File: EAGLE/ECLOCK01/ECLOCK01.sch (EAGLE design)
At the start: 12 parts

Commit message: FInal version of clock PCB before sending to board house
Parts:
- removed JP1: POWER_JACKCOMBO, SparkFun-Connectors:POWER_JACKCOMBO
- removed L1, L2, L3, L4: WS2812B, adafruit:WS2812B
- added C10, C11, C12, C13, C14, C15, C16, C17, C18, C19, C20, C21, C22, C23, C24, C25, C26, C27, C28, C29, C30, C31, C32, C33, C34, C35, C36, C37, C38, C39, C41, C42, C43, C44, C45, C46, C47, C48, C49, C50, C51, C52, C53, C54, C6, C7, C8, C9: 0.1, TinWhiskers:CAPACITOR0805
- added C400, C401: 470, adafruit:CPOL-USE
- added FID1, FID2: FIDUCIAL, TinWhiskers:FIDUCIAL
- added JP2: USB-MICROB, SparkFun-Connectors:USB-MICROB
- added LED1, LED10, LED11, LED12, LED13, LED14, LED15, LED16, LED17, LED18, LED19, LED2, LED20, LED21, LED22, LED23, LED24, LED25, LED26, LED27, LED28, LED29, LED3, LED30, LED31, LED32, LED33, LED34, LED35, LED36, LED37, LED38, LED39, LED4, LED40, LED41, LED42, LED43, LED44, LED45, LED46, LED47, LED48, LED49, LED5, LED50, LED51, LED52, LED53, LED54, LED6, LED7, LED8, LED9: WS2812B, GinWhiskers - temp stuff:WS2812B
- C1, C2, C3: value CAPACITOR0805 -> 0.1
- C4, C5: value 470 -> 0.1; device adafruit:CPOL-USE -> TinWhiskers:CAPACITOR0805
- U$1: device adafruit:ARDUINOUNO -> GinWhiskers - temp stuff:ARDUINOUNO
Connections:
- removed net N$6: L3.DOUT, L4.DIN
- new net N$10: LED15.DOUT, LED16.DIN
- new net N$12: LED18.DIN, LED53.DOUT
- new net N$13: LED19.DOUT, LED20.DIN
- new net N$14: LED17.DIN, LED18.DOUT
- new net N$15: LED19.DIN, LED8.DOUT
- new net N$16: LED47.DOUT, LED49.DIN
- new net N$17: LED39.DOUT, LED50.DIN
- new net N$18: LED24.DOUT, LED25.DIN
- new net N$19: LED25.DOUT, LED26.DIN
- new net N$2: LED11.DOUT, LED12.DIN
- new net N$20: LED13.DOUT, LED24.DIN
- new net N$21: LED27.DOUT, LED28.DIN
- new net N$22: LED28.DOUT, LED29.DIN
- new net N$25: LED40.DOUT, LED41.DIN
- new net N$26: LED20.DOUT, LED21.DIN
- new net N$27: LED11.DIN, LED9.DOUT
- new net N$28: LED17.DOUT, LED5.DIN
- new net N$29: LED4.DIN, LED5.DOUT
- new net N$30: LED6.DOUT, LED7.DIN
- new net N$31: LED7.DOUT, LED8.DIN
- new net N$32: LED21.DOUT, LED32.DIN
- new net N$33: LED48.DIN, LED49.DOUT
- new net N$34: LED36.DIN, LED48.DOUT
- new net N$36: LED37.DOUT, LED38.DIN
- new net N$37: LED38.DOUT, LED39.DIN
- new net N$39: LED30.DOUT, LED53.DIN
- new net N$40: LED34.DOUT, LED45.DIN
- new net N$41: LED32.DOUT, LED33.DIN
- new net N$42: LED33.DOUT, LED34.DIN
- new net N$44: LED31.DIN, LED43.DOUT
- new net N$45: LED4.DOUT, LED6.DIN
- new net N$46: LED46.DOUT, LED47.DIN
- new net N$47: LED45.DOUT, LED46.DIN
- new net N$48: LED42.DOUT, LED44.DIN
- new net N$49: LED43.DIN, LED44.DOUT
- new net N$50: LED30.DIN, LED31.DOUT
- new net N$51: LED41.DOUT, LED42.DIN
- new net N$52: LED35.DIN, LED36.DOUT
- new net N$53: LED35.DOUT, LED54.DIN
- new net N$54: LED50.DOUT, LED51.DIN
- new net N$55: LED51.DOUT, LED52.DIN
- new net N$56: LED23.DIN, LED54.DOUT
- new net N$58: LED22.DIN, LED23.DOUT
- new net N$59: LED14.DIN, LED3.DOUT
- new net N$60: LED10.DIN, LED22.DOUT
- new net N$61: LED10.DOUT, LED9.DIN
- new net N$62: LED29.DOUT, LED40.DIN
- new net N$7: LED12.DOUT, LED13.DIN
- new net N$8: LED26.DOUT, LED37.DIN
- new net N$9: LED14.DOUT, LED15.DIN
- new net VDD: C1.1, C10.1, C11.1, C12.1, C13.1, C14.1, C15.1, C16.1, C17.1, C18.1, C19.1, C2.1, C20.1, C21.1, C22.1, C23.1, C24.1, C25.1, C26.1, C27.1, C28.1, C29.1, C3.1, C30.1, C31.1, C32.1, C33.1, C34.1, C35.1, C36.1, C37.1, C38.1, C39.1, C4.1, C400.+, C401.+, C41.1, C42.1, C43.1, C44.1, C45.1, C46.1, C47.1, C48.1, C49.1, C5.1, C50.1, C51.1, C52.1, C53.1, C54.1, C6.1, C7.1, C8.1, C9.1, JP2.VBUS, LED1.VDD, LED10.VDD, LED11.VDD, LED12.VDD, LED13.VDD, LED14.VDD, LED15.VDD, LED16.VDD, LED17.VDD, LED18.VDD, LED19.VDD, LED2.VDD, LED20.VDD, LED21.VDD, LED22.VDD, LED23.VDD, LED24.VDD, LED25.VDD, LED26.VDD, LED27.VDD, LED28.VDD, LED29.VDD, LED3.VDD, LED30.VDD, LED31.VDD, LED32.VDD, LED33.VDD, LED34.VDD, LED35.VDD, LED36.VDD, LED37.VDD, LED38.VDD, LED39.VDD, LED4.VDD, LED40.VDD, LED41.VDD, LED42.VDD, LED43.VDD, LED44.VDD, LED45.VDD, LED46.VDD, LED47.VDD, LED48.VDD, LED49.VDD, LED5.VDD, LED50.VDD, LED51.VDD, LED52.VDD, LED53.VDD, LED54.VDD, LED6.VDD, LED7.VDD, LED8.VDD, LED9.VDD
- net GND: now also C1.2, C10.2, C11.2, C12.2, C13.2, C14.2, C15.2, C16.2, C17.2, C18.2, C19.2, C2.2, C20.2, C21.2, C22.2, C23.2, C24.2, C25.2, C26.2, C27.2, C28.2, C29.2, C3.2, C30.2, C31.2, C32.2, C33.2, C34.2, C35.2, C36.2, C37.2, C38.2, C39.2, C4.2, C400.-, C401.-, C41.2, C42.2, C43.2, C44.2, C45.2, C46.2, C47.2, C48.2, C49.2, C5.2, C50.2, C51.2, C52.2, C53.2, C54.2, C6.2, C7.2, C8.2, C9.2, JP2.GND, LED1.GND, LED10.GND, LED11.GND, LED12.GND, LED13.GND, LED14.GND, LED15.GND, LED16.GND, LED17.GND, LED18.GND, LED19.GND, LED2.GND, LED20.GND, LED21.GND, LED22.GND, LED23.GND, LED24.GND, LED25.GND, LED26.GND, LED27.GND, LED28.GND, LED29.GND, LED3.GND, LED30.GND, LED31.GND, LED32.GND, LED33.GND, LED34.GND, LED35.GND, LED36.GND, LED37.GND, LED38.GND, LED39.GND, LED4.GND, LED40.GND, LED41.GND, LED42.GND, LED43.GND, LED44.GND, LED45.GND, LED46.GND, LED47.GND, LED48.GND, LED49.GND, LED5.GND, LED50.GND, LED51.GND, LED52.GND, LED53.GND, LED54.GND, LED6.GND, LED7.GND, LED8.GND, LED9.GND; no longer C4.-, C5.-, JP1.GND, JP1.GNDBREAK, L1.GND, L2.GND, L3.GND, L4.GND
- net LED_IN: now also U$1.D13; no longer U$1.D0
- net N$1: now also LED1.DIN; no longer L1.DIN
- net N$3: now also LED1.DOUT, LED2.DIN; no longer L1.DOUT, L2.DIN
- net N$4: now also LED2.DOUT, LED3.DIN; no longer L2.DOUT, L3.DIN
- net N$5: now also LED16.DOUT, LED27.DIN; no longer C4.+, C5.+, JP1.PWR, L1.VDD, L2.VDD, L3.VDD, L4.VDD

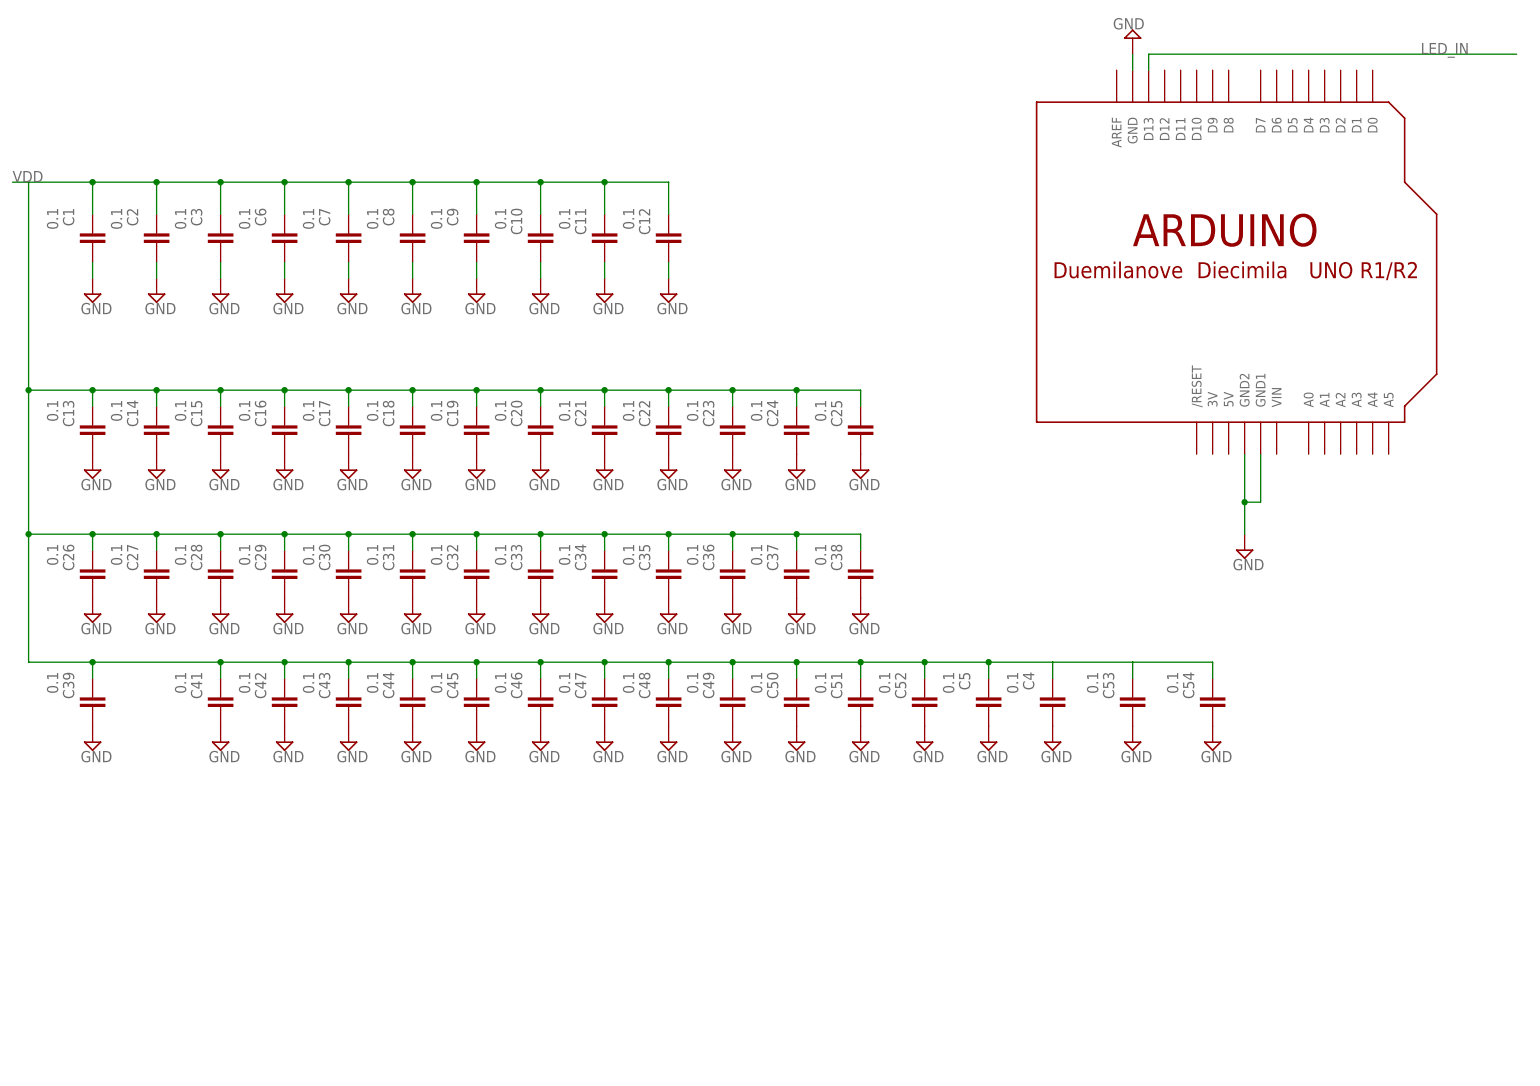
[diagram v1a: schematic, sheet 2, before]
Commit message: Added two pushbuttons and a connector for the horn
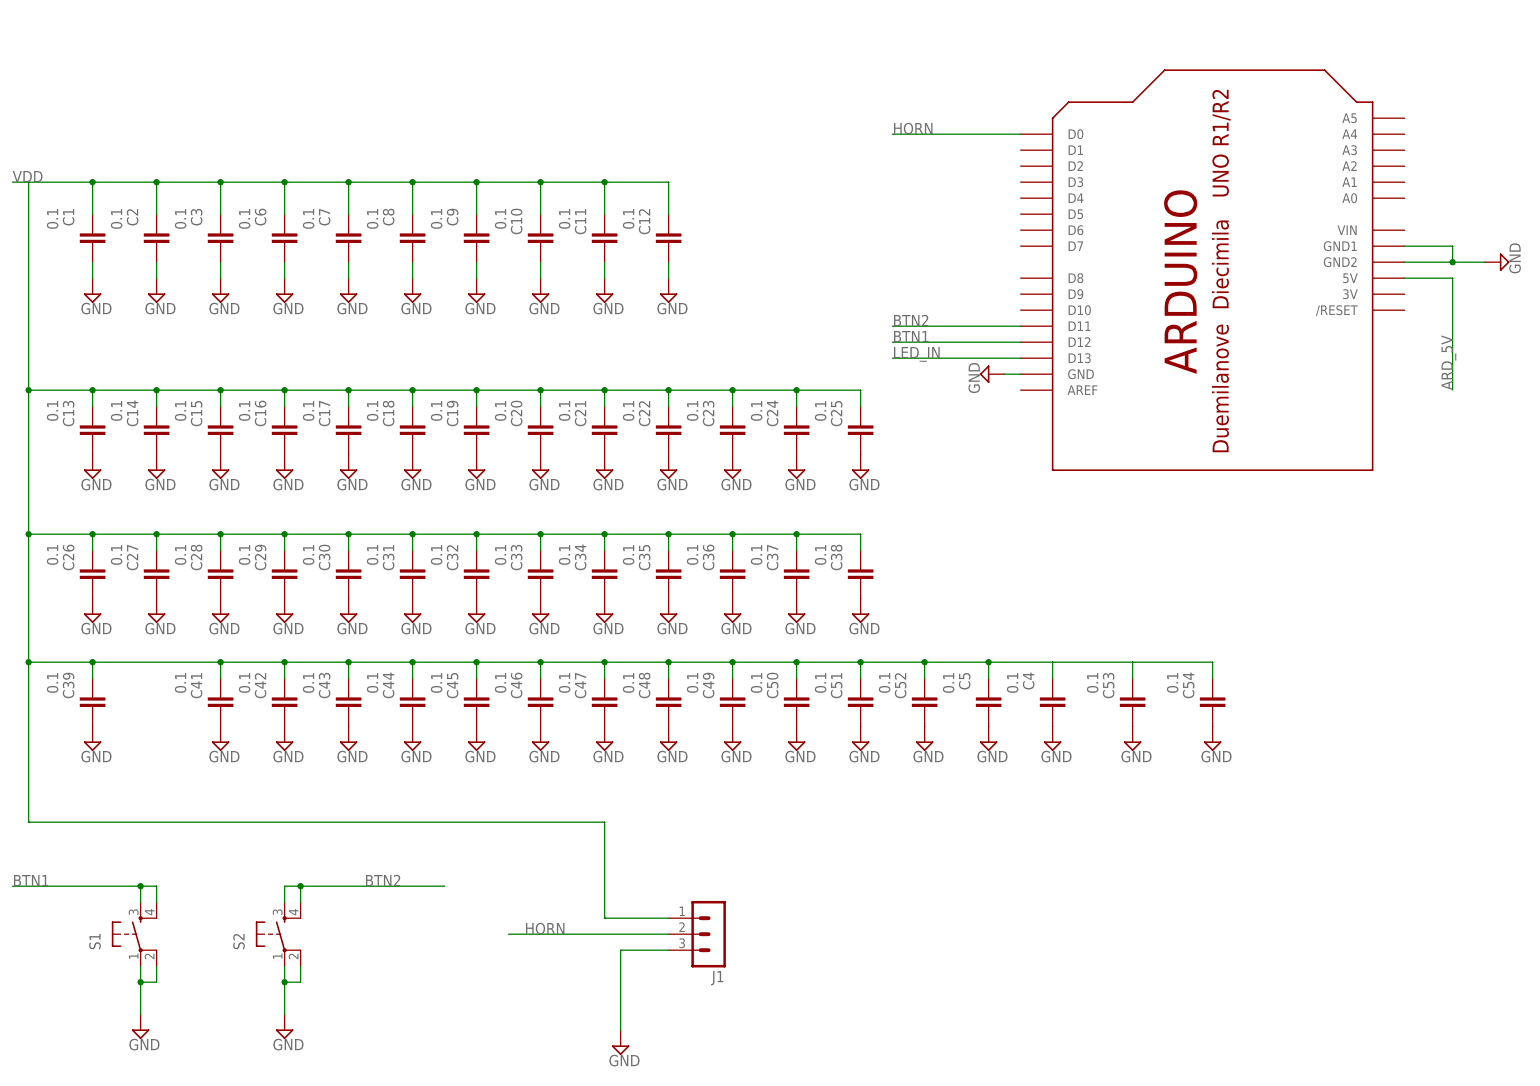
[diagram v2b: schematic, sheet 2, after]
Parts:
- added J1: (no value), !con-lstb:MA03-1
- added S1, S2: (no value), SparkFun:TAC_SWITCHSMD
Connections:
- new net ARD_5V: U$1.5V
- new net BTN1: S1.3, S1.4, U$1.D12
- new net BTN2: S2.3, S2.4, U$1.D11
- new net HORN: J1.2, U$1.D0
- net GND: now also J1.3, S1.1, S1.2, S2.1, S2.2
- net VDD: now also J1.1
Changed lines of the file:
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@@
 </variantdefs>
 <classes>
-<class number="0" name="default" width="0" drill="0">
+<class number="0" name="default" width="0.1524" drill="0.3048">
+<clearance class="0" value="0.1524"/>
+</class>
+<class number="1" name="power" width="0" drill="0">
 </class>
 </classes>
@@
 <part name="SUPPLY112" library="TinWhiskers" deviceset="GND" device=""/>
 <part name="SUPPLY113" library="TinWhiskers" deviceset="GND" device=""/>
+<part name="S1" library="SparkFun" deviceset="TAC_SWITCH" device="SMD"/>
+<part name="S2" library="SparkFun" deviceset="TAC_SWITCH" device="SMD"/>
+<part name="SUPPLY97" library="TinWhiskers" deviceset="GND" device=""/>
+<part name="SUPPLY114" library="TinWhiskers" deviceset="GND" device=""/>
+<part name="J1" library="!con-lstb" deviceset="MA03-1" device=""/>
+<part name="SUPPLY115" library="TinWhiskers" deviceset="GND" device=""/>
 </parts>
 <sheets>
@@
 </plain>
 <instances>
-<instance part="U$1" gate="G$1" x="208.28" y="134.62"/>
-<instance part="SUPPLY8" gate="GND" x="208.28" y="88.9"/>
-<instance part="SUPPLY9" gate="GND" x="190.5" y="170.18" rot="R180"/>
+<instance part="U$1" gate="G$1" x="203.2" y="134.62" rot="R90"/>
+<instance part="SUPPLY8" gate="GND" x="248.92" y="134.62" rot="R90"/>
+<instance part="SUPPLY9" gate="GND" x="167.64" y="116.84" rot="R270"/>
 <instance part="FRAME2" gate="G$1" x="0" y="0"/>
 <instance part="C13" gate="G$1" x="25.4" y="106.68" rot="R270"/>
@@
 <instance part="SUPPLY112" gate="GND" x="190.5" y="58.42"/>
 <instance part="SUPPLY113" gate="GND" x="203.2" y="58.42"/>
+<instance part="S1" gate="S" x="33.02" y="27.94" rot="R90"/>
+<instance part="S2" gate="S" x="55.88" y="27.94" rot="R90"/>
+<instance part="SUPPLY97" gate="GND" x="33.02" y="12.7"/>
+<instance part="SUPPLY114" gate="GND" x="55.88" y="12.7"/>
+<instance part="J1" gate="G$1" x="124.46" y="27.94" rot="R180"/>
+<instance part="SUPPLY115" gate="GND" x="109.22" y="10.16"/>
 </instances>
 <busses>
@@
 <pinref part="U$1" gate="G$1" pin="GND2"/>
 <pinref part="SUPPLY8" gate="GND" pin="GND"/>
-<wire x1="208.28" y1="104.14" x2="208.28" y2="96.52" width="0.1524" layer="91"/>
+<wire x1="233.68" y1="134.62" x2="241.3" y2="134.62" width="0.1524" layer="91"/>
 <pinref part="U$1" gate="G$1" pin="GND1"/>
-<wire x1="208.28" y1="96.52" x2="208.28" y2="91.44" width="0.1524" layer="91"/>
-<wire x1="210.82" y1="104.14" x2="210.82" y2="96.52" width="0.1524" layer="91"/>
-<wire x1="210.82" y1="96.52" x2="208.28" y2="96.52" width="0.1524" layer="91"/>
-<junction x="208.28" y="96.52"/>
+<wire x1="241.3" y1="134.62" x2="246.38" y2="134.62" width="0.1524" layer="91"/>
+<wire x1="233.68" y1="137.16" x2="241.3" y2="137.16" width="0.1524" layer="91"/>
+<wire x1="241.3" y1="137.16" x2="241.3" y2="134.62" width="0.1524" layer="91"/>
+<junction x="241.3" y="134.62"/>
 </segment>
 <segment>
 <pinref part="SUPPLY9" gate="GND" pin="GND"/>
 <pinref part="U$1" gate="G$1" pin="GND"/>
-<wire x1="190.5" y1="167.64" x2="190.5" y2="165.1" width="0.1524" layer="91"/>
+<wire x1="170.18" y1="116.84" x2="172.72" y2="116.84" width="0.1524" layer="91"/>
 </segment>
 <segment>
@@
 <pinref part="SUPPLY113" gate="GND" pin="GND"/>
 </segment>
+<segment>
+<pinref part="S1" gate="S" pin="1"/>
+<wire x1="33.02" y1="22.86" x2="33.02" y2="20.32" width="0.1524" layer="91"/>
+<pinref part="S1" gate="S" pin="2"/>
+<wire x1="33.02" y1="20.32" x2="35.56" y2="20.32" width="0.1524" layer="91"/>
+<wire x1="35.56" y1="20.32" x2="35.56" y2="22.86" width="0.1524" layer="91"/>
+<wire x1="33.02" y1="20.32" x2="33.02" y2="15.24" width="0.1524" layer="91"/>
+<pinref part="SUPPLY97" gate="GND" pin="GND"/>
+<junction x="33.02" y="20.32"/>
+</segment>
+<segment>
+<pinref part="S2" gate="S" pin="1"/>
+<wire x1="55.88" y1="22.86" x2="55.88" y2="20.32" width="0.1524" layer="91"/>
+<pinref part="S2" gate="S" pin="2"/>
+<wire x1="55.88" y1="20.32" x2="58.42" y2="20.32" width="0.1524" layer="91"/>
+<wire x1="58.42" y1="20.32" x2="58.42" y2="22.86" width="0.1524" layer="91"/>
+<wire x1="55.88" y1="20.32" x2="55.88" y2="15.24" width="0.1524" layer="91"/>
+<pinref part="SUPPLY114" gate="GND" pin="GND"/>
+<junction x="55.88" y="20.32"/>
+</segment>
+<segment>
+<pinref part="J1" gate="G$1" pin="3"/>
+<wire x1="116.84" y1="25.4" x2="109.22" y2="25.4" width="0.1524" layer="91"/>
+<wire x1="109.22" y1="25.4" x2="109.22" y2="12.7" width="0.1524" layer="91"/>
+<pinref part="SUPPLY115" gate="GND" pin="GND"/>
+</segment>
 </net>
 <net name="LED_IN" class="0">
 <segment>
-<label x="236.22" y="167.64" size="1.778" layer="95"/>
+<label x="152.4" y="119.38" size="1.778" layer="95"/>
 <pinref part="U$1" gate="G$1" pin="D13"/>
-<wire x1="251.46" y1="167.64" x2="193.04" y2="167.64" width="0.1524" layer="91"/>
-<wire x1="193.04" y1="167.64" x2="193.04" y2="165.1" width="0.1524" layer="91"/>
+<wire x1="152.4" y1="119.38" x2="172.72" y2="119.38" width="0.1524" layer="91"/>
 </segment>
 </net>
@@
 <wire x1="203.2" y1="68.58" x2="203.2" y2="71.12" width="0.1524" layer="91"/>
 <wire x1="203.2" y1="71.12" x2="190.5" y2="71.12" width="0.1524" layer="91"/>
-</segment>
-</net>
+<wire x1="116.84" y1="30.48" x2="106.68" y2="30.48" width="0.1524" layer="91"/>
+<wire x1="106.68" y1="30.48" x2="106.68" y2="45.72" width="0.1524" layer="91"/>
+<wire x1="106.68" y1="45.72" x2="15.24" y2="45.72" width="0.1524" layer="91"/>
+<wire x1="15.24" y1="45.72" x2="15.24" y2="71.12" width="0.1524" layer="91"/>
+<junction x="15.24" y="71.12"/>
+<pinref part="J1" gate="G$1" pin="1"/>
+</segment>
+</net>
+<net name="BTN2" class="0">
+<segment>
+<pinref part="S2" gate="S" pin="3"/>
+<wire x1="55.88" y1="33.02" x2="55.88" y2="35.56" width="0.1524" layer="91"/>
+<pinref part="S2" gate="S" pin="4"/>
+<wire x1="55.88" y1="35.56" x2="58.42" y2="35.56" width="0.1524" layer="91"/>
+<wire x1="58.42" y1="35.56" x2="58.42" y2="33.02" width="0.1524" layer="91"/>
+<wire x1="58.42" y1="35.56" x2="81.28" y2="35.56" width="0.1524" layer="91"/>
+<junction x="58.42" y="35.56"/>
+<label x="68.58" y="35.56" size="1.778" layer="95"/>
+</segment>
+<segment>
+<pinref part="U$1" gate="G$1" pin="D11"/>
+<wire x1="172.72" y1="124.46" x2="152.4" y2="124.46" width="0.1524" layer="91"/>
+<label x="152.4" y="124.46" size="1.778" layer="95"/>
+</segment>
+</net>
+<net name="BTN1" class="0">
+<segment>
+<pinref part="S1" gate="S" pin="3"/>
+<wire x1="33.02" y1="33.02" x2="33.02" y2="35.56" width="0.1524" layer="91"/>
+<pinref part="S1" gate="S" pin="4"/>
+<wire x1="33.02" y1="35.56" x2="35.56" y2="35.56" width="0.1524" layer="91"/>
+<wire x1="35.56" y1="35.56" x2="35.56" y2="33.02" width="0.1524" layer="91"/>
+<junction x="33.02" y="35.56"/>
+<wire x1="33.02" y1="35.56" x2="12.7" y2="35.56" width="0.1524" layer="91"/>
+<label x="12.7" y="35.56" size="1.778" layer="95"/>
+</segment>
+<segment>
+<pinref part="U$1" gate="G$1" pin="D12"/>
+<wire x1="172.72" y1="121.92" x2="152.4" y2="121.92" width="0.1524" layer="91"/>
+<label x="152.4" y="121.92" size="1.778" layer="95"/>
+</segment>
+</net>
+<net name="ARD_5V" class="0">
+<segment>
+<pinref part="U$1" gate="G$1" pin="5V"/>
+<wire x1="233.68" y1="132.08" x2="241.3" y2="132.08" width="0.1524" layer="91"/>
+<wire x1="241.3" y1="132.08" x2="241.3" y2="114.3" width="0.1524" layer="91"/>
+<label x="241.3" y="114.3" size="1.778" layer="95" rot="R90"/>
+</segment>
+</net>
+<net name="HORN" class="0">
+<segment>
+<pinref part="J1" gate="G$1" pin="2"/>
+<wire x1="116.84" y1="27.94" x2="91.44" y2="27.94" width="0.1524" layer="91"/>
+<label x="93.98" y="27.94" size="1.778" layer="95"/>
+</segment>
+<segment>
+<label x="152.4" y="154.94" size="1.778" layer="95"/>
+<pinref part="U$1" gate="G$1" pin="D0"/>
+<wire x1="172.72" y1="154.94" x2="152.4" y2="154.94" width="0.1524" layer="91"/>
+</segment>
+</net>
